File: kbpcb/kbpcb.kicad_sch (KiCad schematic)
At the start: 18 parts

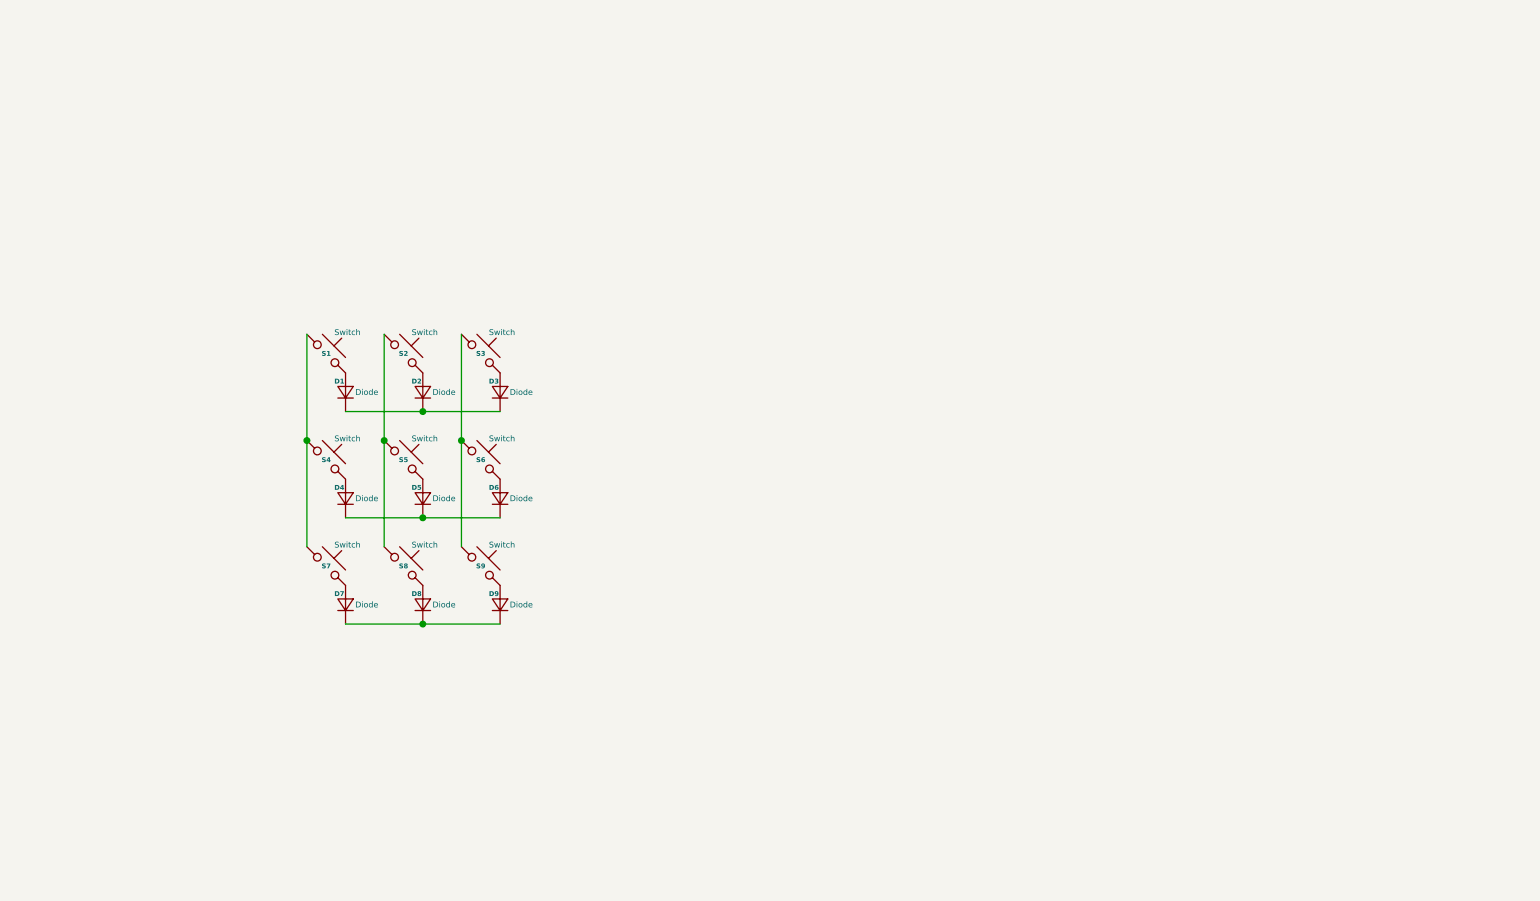
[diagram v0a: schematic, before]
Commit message: placed rp2040 zero and all switches
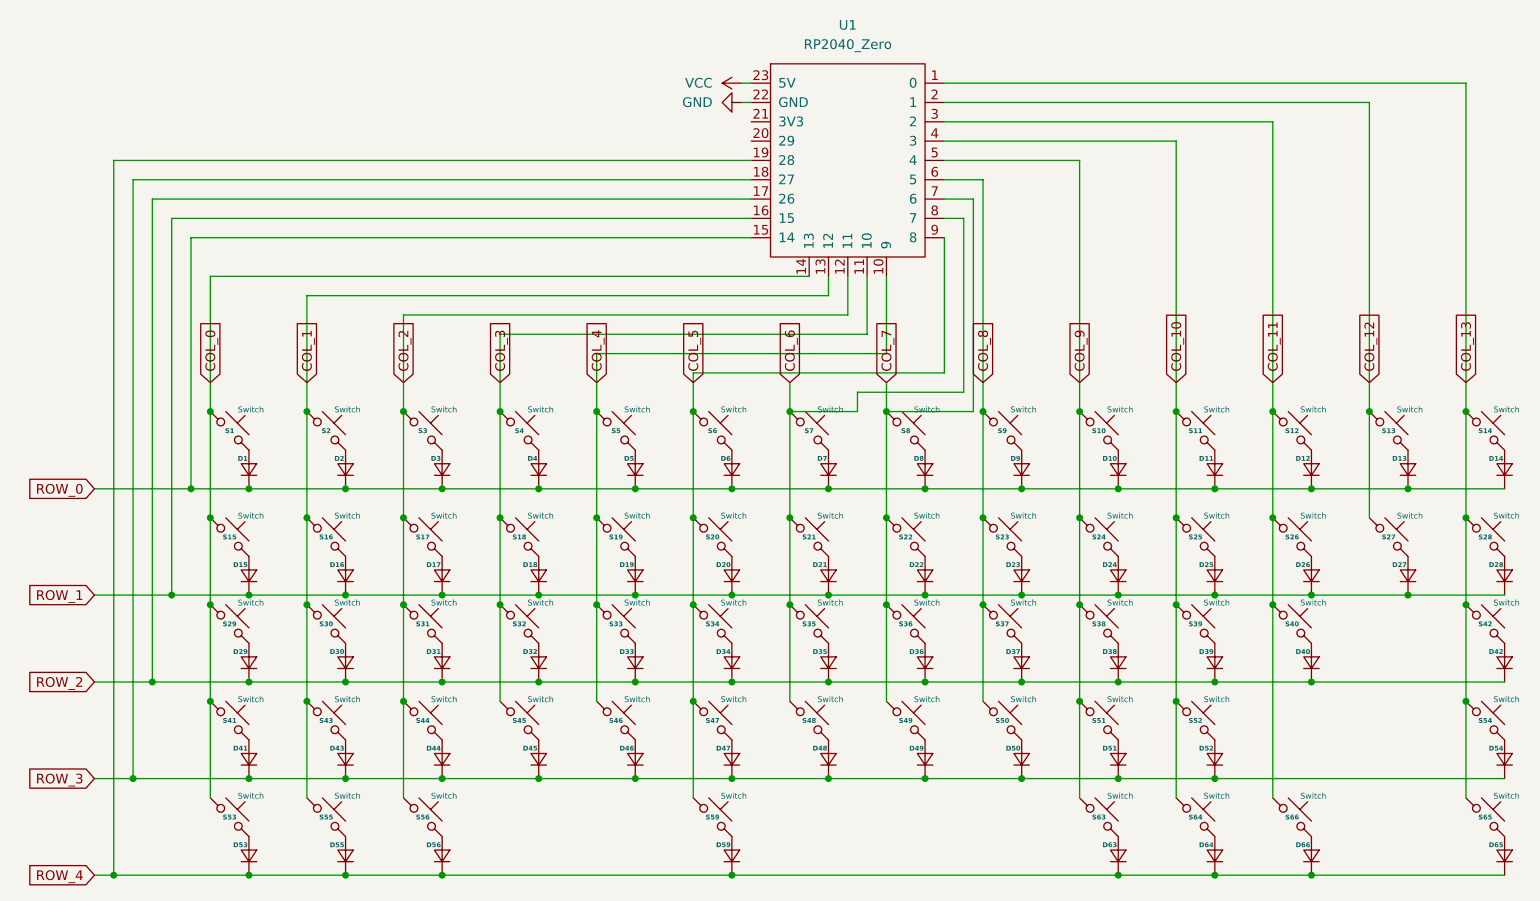
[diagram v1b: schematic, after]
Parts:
- added D10, D11, D12, D13, D14, D15, D16, D17, D18, D19, D20, D21, D22, D23, D24, D25, D26, D27, D28, D29, D30, D31, D32, D33, D34, D35, D36, D37, D38, D39, D40, D41, D42, D43, D44, D45, D46, D47, D48, D49, D50, D51, D52, D53, D54, D55, D56, D59, D63, D64, D65, D66: Diode, Diode_THT:D_DO-35_SOD27_P7.62mm_Horizontal, symbol ScottoKeebs:Placeholder_Diode
- added S10, S11, S12, S13, S14, S15, S16, S17, S18, S19, S20, S21, S22, S23, S24, S25, S26, S27, S28, S29, S30, S31, S32, S33, S34, S35, S36, S37, S38, S39, S40, S41, S42, S43, S44, S45, S46, S47, S48, S49, S50, S51, S52, S53, S54, S55, S56, S59, S63, S64, S65, S66: Switch, CherryMX:CherryMX_1.00u, symbol ScottoKeebs:Placeholder_Keyswitch
- added U1: RP2040_Zero, ScottoKeebs_MCU:RP2040_Zero, symbol ScottoKeebs:MCU_RP2040_Zero
- D1, D2, D3, D4, D5, D6, D7, D8, D9: footprint (none) -> Diode_THT:D_DO-35_SOD27_P7.62mm_Horizontal
- S1, S2, S3, S4, S5, S6, S7, S8, S9: footprint (none) -> CherryMX:CherryMX_1.00u
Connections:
- net ROW_0: now reaches D4.1 (K), D5.1 (K), D6.1 (K)
- net ROW_0: now also D1.1 (K), D2.1 (K), D3.1 (K), D7.1 (K), D8.1 (K), D9.1 (K), D10.1 (K), D11.1 (K), D12.1 (K), D13.1 (K), D14.1 (K), U1.15 (14)
- new net: D51.2 (A), S51.2
- new net: D63.2 (A), S63.2
- new net: D53.2 (A), S53.2
- new net: D21.2 (A), S21.2
- new net: D16.2 (A), S16.2
- new net: D33.2 (A), S33.2
- new net: D55.2 (A), S55.2
- new net: D41.2 (A), S41.2
- new net: D66.2 (A), S66.2
- new net: D34.2 (A), S34.2
- new net: D10.2 (A), S10.2
- new net: D13.2 (A), S13.2
- new net: D36.2 (A), S36.2
- new net: D12.2 (A), S12.2
- new net: D19.2 (A), S19.2
- new net: D42.2 (A), S42.2
- new net: D28.2 (A), S28.2
- new net: D43.2 (A), S43.2
- new net: D49.2 (A), S49.2
- new net: D65.2 (A), S65.2
- new net: D59.2 (A), S59.2
- new net: D26.2 (A), S26.2
- new net: D23.2 (A), S23.2
- new net: D35.2 (A), S35.2
- new net: D24.2 (A), S24.2
- new net: D29.2 (A), S29.2
- new net: D45.2 (A), S45.2
- new net: D27.2 (A), S27.2
- new net: D39.2 (A), S39.2
- new net: D18.2 (A), S18.2
- new net: D37.2 (A), S37.2
- new net: D30.2 (A), S30.2
- new net: D31.2 (A), S31.2
- new net: D20.2 (A), S20.2
- new net: D64.2 (A), S64.2
- new net: D11.2 (A), S11.2
- new net: D40.2 (A), S40.2
- new net: D44.2 (A), S44.2
- new net: D32.2 (A), S32.2
- new net: D54.2 (A), S54.2
- new net: D15.2 (A), S15.2
- new net: D46.2 (A), S46.2
- new net: D17.2 (A), S17.2
- new net: D56.2 (A), S56.2
- new net: D47.2 (A), S47.2
- new net: D52.2 (A), S52.2
- new net: D50.2 (A), S50.2
- new net: D14.2 (A), S14.2
- new net: D25.2 (A), S25.2
- new net: D38.2 (A), S38.2
- new net: D48.2 (A), S48.2
- new net: D22.2 (A), S22.2
- new net COL_0: S1.1, S15.1, S29.1, S41.1, S53.1, U1.14 (13)
- new net COL_1: S16.1, S2.1, S30.1, S43.1, S55.1, U1.13 (12)
- new net COL_10: S11.1, S25.1, S39.1, S52.1, S64.1, U1.4 (3)
- new net COL_11: S12.1, S26.1, S40.1, S66.1, U1.3 (2)
- new net COL_12: S13.1, S27.1, U1.2 (1)
- new net COL_13: S14.1, S28.1, S42.1, S54.1, S65.1, U1.1 (0)
- new net COL_2: S17.1, S3.1, S31.1, S44.1, S56.1, U1.12 (11)
- new net COL_3: S18.1, S32.1, S4.1, S45.1, U1.11 (10)
- new net COL_4: S19.1, S33.1, S46.1, S5.1, U1.10 (9)
- new net COL_5: S20.1, S34.1, S47.1, S59.1, S6.1, U1.9 (8)
- new net COL_6: S21.1, S35.1, S48.1, S7.1, U1.8 (7)
- new net COL_7: S22.1, S36.1, S49.1, S8.1, U1.7 (6)
- new net COL_8: S23.1, S37.1, S50.1, S9.1, U1.6 (5)
- new net COL_9: S10.1, S24.1, S38.1, S51.1, S63.1, U1.5 (4)
- new net GND: U1.22 (GND)
- new net ROW_1: D15.1 (K), D16.1 (K), D17.1 (K), D18.1 (K), D19.1 (K), D20.1 (K), D21.1 (K), D22.1 (K), D23.1 (K), D24.1 (K), D25.1 (K), D26.1 (K), D27.1 (K), D28.1 (K), U1.16 (15)
- new net ROW_2: D29.1 (K), D30.1 (K), D31.1 (K), D32.1 (K), D33.1 (K), D34.1 (K), D35.1 (K), D36.1 (K), D37.1 (K), D38.1 (K), D39.1 (K), D40.1 (K), D42.1 (K), U1.17 (26)
- new net ROW_3: D41.1 (K), D43.1 (K), D44.1 (K), D45.1 (K), D46.1 (K), D47.1 (K), D48.1 (K), D49.1 (K), D50.1 (K), D51.1 (K), D52.1 (K), D54.1 (K), U1.18 (27)
- new net ROW_4: D53.1 (K), D55.1 (K), D56.1 (K), D59.1 (K), D63.1 (K), D64.1 (K), D65.1 (K), D66.1 (K), U1.19 (28)
- new net VCC: U1.23 (5V)
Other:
- moved on the sheet: D1, S1

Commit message: layout changes
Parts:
- removed D54: Diode, Diode_THT:D_DO-35_SOD27_P7.62mm_Horizontal, symbol ScottoKeebs:Placeholder_Diode
- added D1, D100, D101, D102, D103, D104, D105, D106, D107, D108, D109, D110, D111, D112, D113, D114, D115, D116, D117, D118, D119, D120, D121, D122, D123, D124, D125, D126, D127, D128, D129, D130, D131, D132, D133, D134, D135, D136, D137, D138, D139, D140, D141, D142, D143, D144, D145, D146, D147, D148, D149, D150, D151, D152, D153, D154, D155, D156, D157, D158, D159, D160, D161, D162, D163, D164, D165, D166, D167, D168, D169, D170, D171, D172, D173, D174, D175, D176, D177, D178, D179, D180, D181, D182, D183, D184, D185, D186, D187, D188, D189, D2, D3, D4, D41, D5, D55, D56, D57, D6, D60, D61, D63, D64, D69, D7, D70, D71, D72, D73, D74, D75, D76, D77, D78, D79, D8, D80, D81, D82, D83, D84, D85, D86, D87, D88, D89, D90, D91, D92, D93, D94, D95, D96, D97, D98, D99: Diode, Diode_THT:D_DO-35_SOD27_P7.62mm_Horizontal, symbol ScottoKeebs:Placeholder_Diode
- added DS1: OLED_128X64_1.3_I2C, OLED_128X64_1.3_I2C:LCD_OLED_128X64_1.3_I2C, symbol OLED_128X64_1.3_I2C:OLED_128X64_1.3_I2C
- added S1, S100, S101, S102, S103, S104, S105, S106, S107, S108, S109, S110, S111, S112, S113, S114, S115, S116, S117, S118, S119, S120, S121, S122, S123, S124, S125, S126, S127, S128, S129, S130, S131, S132, S133, S134, S135, S136, S137, S138, S139, S140, S141, S142, S143, S144, S145, S146, S147, S148, S149, S150, S151, S152, S153, S154, S155, S156, S157, S158, S159, S160, S161, S162, S163, S164, S165, S166, S167, S168, S169, S170, S171, S172, S173, S174, S175, S176, S177, S178, S179, S180, S181, S182, S183, S184, S185, S186, S187, S188, S189, S2, S3, S4, S41, S5, S55, S56, S6, S60, S61, S63, S64, S69, S7, S70, S71, S72, S73, S74, S75, S76, S77, S78, S79, S8, S80, S81, S82, S83, S84, S85, S86, S87, S88, S89, S90, S91, S92, S93, S94, S95, S96, S97, S98, S99: Switch, CherryMX:CherryMX_1.00u, symbol ScottoKeebs:Placeholder_Keyswitch
- added U2: Teensy4.1, symbol teensy:Teensy4.1
- added U3, U4: TRRS, ScottoKeebs_Components:TRRS_PJ-320A, symbol ScottoKeebs:Placeholder_TRRS
- renumbered D41 to D43, D43 to D44, D44 to D45, D45 to D46, D46 to D47, D47 to D48, D48 to D49, D49 to D50, D50 to D51, D51 to D52, D52 to D53, D53 to D54, D55 to D58, D56 to D59, D59 to D62, D63 to D66, D64 to D67, D66 to D68, S41 to S43, S43 to S44, S44 to S45, S45 to S46, S46 to S47, S47 to S48, S48 to S49, S49 to S50, S50 to S51, S51 to S52, S52 to S53, S53 to S57, S55 to S58, S56 to S59, S59 to S62, S63 to S66, S64 to S67, S66 to S68
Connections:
- net COL_0: now also U1.3 (2), S1.1, S102.1, S110.1, S41.1, S69.1, S78.1, S86.1, S94.1, U2.2 (0_RX1_CRX2_CS1); no longer U1.14 (13)
- net COL_1: now also S54.1, U1.4 (3), S103.1, S111.1, S2.1, S71.1, S79.1, S87.1, S95.1, U2.3 (1_TX1_CTX2_MISO1); no longer U1.13 (12)
- net COL_10: now also U1.14 (13), U2.12 (10_CS_MQSR); no longer U1.4 (3)
- net COL_11: now also U1.15 (14), U2.13 (11_MOSI_CTX1); no longer U1.3 (2)
- net COL_12: now also U1.16 (15), U2.14 (12_MISO_MQSL); no longer U1.2 (1)
- net COL_13: now also U1.17 (26), S56.1, S70.1, U2.36 (14_A0_TX3_SPDIF_OUT); no longer S54.1, S65.1, U1.1 (0)
- net COL_2: now also U1.5 (4), U1.6 (5), S104.1, S112.1, S3.1, S55.1, S72.1, S80.1, S88.1, S96.1, U2.4 (2_OUT2); no longer U1.12 (11)
- net COL_3: now also U1.7 (6), S105.1, S113.1, S4.1, S60.1, S73.1, S81.1, S89.1, S97.1, U2.5 (3_LRCLK2); no longer U1.11 (10)
- net COL_4: now also U1.8 (7), S106.1, S114.1, S5.1, S61.1, S74.1, S82.1, S90.1, S98.1, U2.6 (4_BCLK2); no longer U1.10 (9)
- net COL_5: now also S107.1, S6.1, S63.1, S75.1, S83.1, S91.1, S99.1, U2.7 (5_IN2)
- net COL_6: now also U1.10 (9), S100.1, S108.1, S64.1, S7.1, S76.1, S84.1, S92.1, U2.8 (6_OUT1D); no longer U1.8 (7)
- net COL_7: now also S65.1, U1.11 (10), S101.1, S109.1, S77.1, S8.1, S85.1, S93.1, U2.9 (7_RX2_OUT1A); no longer U1.7 (6)
- net COL_8: now also U1.12 (11), U2.10 (8_TX2_IN1); no longer U1.6 (5)
- net COL_9: now also U1.13 (12), U2.11 (9_OUT1C); no longer U1.5 (4)
- net GND: now also DS1.2 (GND), U2.47 (GND), U4.1 (SLEEVE)
- net ROW_0: now also D1.1 (K), D2.1 (K), D3.1 (K), D4.1 (K), D5.1 (K), D6.1 (K), D7.1 (K), D8.1 (K), U2.37 (15_A1_RX3_SPDIF_IN); no longer U1.15 (14)
- net ROW_1: now also D65.1 (K), D41.1 (K), D55.1 (K), D60.1 (K), D61.1 (K), D63.1 (K), D64.1 (K), D69.1 (K), U2.38 (16_A2_RX4_SCL1); no longer U1.16 (15)
- net ROW_2: now also D71.1 (K), D72.1 (K), D73.1 (K), D74.1 (K), D75.1 (K), D76.1 (K), D77.1 (K), D78.1 (K), U2.39 (17_A3_TX4_SDA1); no longer U1.17 (26)
- net ROW_3: now also D56.1 (K), D79.1 (K), D80.1 (K), D81.1 (K), D82.1 (K), D83.1 (K), D84.1 (K), D85.1 (K), D86.1 (K), U2.40 (18_A4_SDA); no longer U1.18 (27)
- net ROW_4: now also D70.1 (K), D87.1 (K), D88.1 (K), D89.1 (K), D90.1 (K), D91.1 (K), D92.1 (K), D93.1 (K), D94.1 (K), U2.41 (19_A5_SCL); no longer D65.1 (K), U1.19 (28)
- net VCC: now also U2.48 (VIN), U4.2 (TIP); no longer U1.23 (5V)
- net at S65.2: now also D69.2 (A); no longer D65.2 (A)
- net at S54.2: now also D55.2 (A)
- net +3V3: now reaches U1.21 (3V3)
- new net: D144.2 (A), S143.2
- new net: D173.2 (A), S172.2
- new net: D100.2 (A), S99.2
- new net: D72.2 (A), S71.2
- new net: D183.2 (A), S183.2
- new net: D168.2 (A), S167.2
- new net: D103.2 (A), S102.2
- new net: D94.2 (A), S93.2
- new net: D83.2 (A), S82.2
- new net: D139.2 (A), S138.2
- new net: D70.2 (A), S70.2
- new net: D99.2 (A), S98.2
- new net: D175.2 (A), S174.2
- new net: D121.2 (A), S120.2
- new net: D177.2 (A), S176.2
- new net: D153.2 (A), S152.2
- new net: D90.2 (A), S89.2
- new net: D117.2 (A), S116.2
- new net: D64.2 (A), S63.2
- new net: D2.2 (A), S2.2
- new net: D160.2 (A), S159.2
- new net: D114.2 (A), S113.2
- new net: D170.2 (A), S169.2
- new net: D187.2 (A), S187.2
- new net: D76.2 (A), S75.2
- new net: D60.2 (A), S55.2
- new net: D124.2 (A), S123.2
- new net: D128.2 (A), S127.2
- new net: D1.2 (A), S1.2
- new net: D88.2 (A), S87.2
- new net: D123.2 (A), S122.2
- new net: D135.2 (A), S134.2
- new net: D41.2 (A), S41.2
- new net: D112.2 (A), S111.2
- new net: D148.2 (A), S147.2
- new net: D151.2 (A), S150.2
- new net: D181.2 (A), S180.2
- new net: D113.2 (A), S112.2
- new net: D115.2 (A), S114.2
- new net: D57.2 (A), S181.2
- new net: D184.2 (A), S184.2
- new net: D159.2 (A), S158.2
- new net: D86.2 (A), S85.2
- new net: D155.2 (A), S154.2
- new net: D85.2 (A), S84.2
- new net: D152.2 (A), S151.2
- new net: D166.2 (A), S165.2
- new net: D163.2 (A), S162.2
- new net: D141.2 (A), S140.2
- new net: D108.2 (A), S107.2
- new net: D106.2 (A), S105.2
- new net: D116.2 (A), S115.2
- new net: D127.2 (A), S126.2
- new net: D133.2 (A), S132.2
- new net: D161.2 (A), S160.2
- new net: D129.2 (A), S128.2
- new net: D92.2 (A), S91.2
- new net: D7.2 (A), S7.2
- new net: D5.2 (A), S5.2
- new net: D178.2 (A), S177.2
- new net: D101.2 (A), S100.2
- new net: D179.2 (A), S178.2
- new net: D130.2 (A), S129.2
- new net: S124.1, S130.1, S136.1, S142.1, S148.1
- new net: D125.2 (A), S124.2
- new net: D138.2 (A), S137.2
- new net: D176.2 (A), S175.2
- new net: D180.2 (A), S179.2
- new net: D165.2 (A), S164.2
- new net: D105.2 (A), S104.2
- new net: D146.2 (A), S145.2
- new net: D174.2 (A), S173.2
- new net: D188.2 (A), S188.2
- new net: D78.2 (A), S77.2
- new net: D118.2 (A), S117.2
- new net: D79.2 (A), S78.2
- new net: D56.2 (A), S56.2
- new net: D63.2 (A), S61.2
- new net: D150.2 (A), S149.2
- new net: D75.2 (A), S74.2
- new net: D134.2 (A), S133.2
- new net: D102.2 (A), S101.2
- new net: D149.2 (A), S148.2
- new net: D96.2 (A), S95.2
- new net: D122.2 (A), S121.2
- new net: D77.2 (A), S76.2
- new net: D137.2 (A), S136.2
- new net: D91.2 (A), S90.2
- new net: D164.2 (A), S163.2
- new net: D110.2 (A), S109.2
- new net: D104.2 (A), S103.2
- new net: D158.2 (A), S157.2
- new net: D172.2 (A), S171.2
- new net: D87.2 (A), S86.2
- new net: D189.2 (A), S189.2
- new net: D81.2 (A), S80.2
- new net: D71.2 (A), S69.2
- new net: D136.2 (A), S135.2
- new net: D157.2 (A), S156.2
- new net: D74.2 (A), S73.2
- new net: D6.2 (A), S6.2
- new net: D84.2 (A), S83.2
- new net: D132.2 (A), S131.2
- new net: D4.2 (A), S4.2
- new net: D111.2 (A), S110.2
- new net: D97.2 (A), S96.2
- new net: D182.2 (A), S182.2
- new net: D80.2 (A), S79.2
- new net: D167.2 (A), S166.2
- new net: D131.2 (A), S130.2
- new net: D185.2 (A), S185.2
- new net: D186.2 (A), S186.2
- new net: D8.2 (A), S8.2
- new net: D162.2 (A), S161.2
- new net: D142.2 (A), S141.2
- new net: D73.2 (A), S72.2
- new net: D65.2 (A), S64.2
- new net: D143.2 (A), S142.2
- new net: D126.2 (A), S125.2
- new net: D120.2 (A), S119.2
- new net: D169.2 (A), S168.2
- new net: D171.2 (A), S170.2
- new net: D61.2 (A), S60.2
- new net: D93.2 (A), S92.2
- new net: D109.2 (A), S108.2
- new net: D98.2 (A), S97.2
- new net: D95.2 (A), S94.2
- new net: D147.2 (A), S146.2
- new net: D107.2 (A), S106.2
- new net: D89.2 (A), S88.2
- new net: D3.2 (A), S3.2
- new net: D154.2 (A), S153.2
- new net: D119.2 (A), S118.2
- new net: D156.2 (A), S155.2
- new net: D140.2 (A), S139.2
- new net: D145.2 (A), S144.2
- new net: D82.2 (A), S81.2
- new net LEFT_COL_0: S176.1, S181.1, S182.1, S183.1
- new net LEFT_COL_1: S174.1, S175.1, S177.1, S178.1, S180.1, S184.1, S185.1, S186.1
- new net LEFT_COL_2: S169.1, S170.1, S171.1, S172.1, S173.1, S187.1, S188.1, S189.1
- new net LEFT_COL_3: S165.1, S166.1, S167.1, S168.1, S179.1
- new net LEFT_COL_4: S160.1, S161.1, S162.1, S163.1, S164.1
- new net LEFT_COL_5: S155.1, S156.1, S157.1, S158.1, S159.1
- new net LEFT_COL_6: S150.1, S151.1, S152.1, S153.1, S154.1
- new net LEFT_COL_7: S131.1, S137.1, S143.1, S147.1, S149.1
- new net LEFT_ROW_0: D132.1 (K), D151.1 (K), D156.1 (K), D161.1 (K), D166.1 (K), D170.1 (K), D175.1 (K), D184.1 (K), D187.1 (K), D57.1 (K)
- new net LEFT_ROW_1: D138.1 (K), D152.1 (K), D157.1 (K), D162.1 (K), D167.1 (K), D171.1 (K), D176.1 (K), D177.1 (K), D182.1 (K), D185.1 (K), D188.1 (K)
- new net LEFT_ROW_2: D144.1 (K), D153.1 (K), D158.1 (K), D163.1 (K), D168.1 (K), D172.1 (K), D178.1 (K), D183.1 (K), D186.1 (K), D189.1 (K)
- new net LEFT_ROW_3: D148.1 (K), D154.1 (K), D159.1 (K), D164.1 (K), D169.1 (K), D173.1 (K), D179.1 (K)
- new net LEFT_ROW_4: D150.1 (K), D155.1 (K), D160.1 (K), D165.1 (K), D174.1 (K), D180.1 (K), D181.1 (K)
- new net MID_COL_0: S115.1, S116.1, S117.1, S118.1, S119.1
- new net MID_COL_1: S120.1, S126.1, S132.1, S138.1, S144.1
- new net MID_COL_2: S121.1, S127.1, S133.1, S139.1, S145.1
- new net MID_COL_3: S122.1, S128.1, S134.1, S140.1, S146.1
- new net MID_COL_4: S123.1, S129.1, S135.1, S141.1
- new net MID_COL_6: S125.1
- new net MID_ROW_0: D116.1 (K), D121.1 (K), D122.1 (K), D123.1 (K), D124.1 (K), D125.1 (K), D126.1 (K)
- new net MID_ROW_1: D117.1 (K), D127.1 (K), D128.1 (K), D129.1 (K), D130.1 (K), D131.1 (K)
- new net MID_ROW_2: D118.1 (K), D133.1 (K), D134.1 (K), D135.1 (K), D136.1 (K), D137.1 (K)
- new net MID_ROW_3: D119.1 (K), D139.1 (K), D140.1 (K), D141.1 (K), D142.1 (K), D143.1 (K)
- new net MID_ROW_4: D120.1 (K), D145.1 (K), D146.1 (K), D147.1 (K), D149.1 (K)
- new net OLED_3V3: U2.15 (3V3)
- new net OLED_SCL: DS1.3 (SCK), U2.16 (24_A10_TX6_SCL2)
- new net OLED_SDA: DS1.4 (SDA), U2.17 (25_A11_RX6_SDA2)
- new net RIGHT_SCL: U1.2 (1), U4.4 (RING2)
- new net RIGHT_SDA: U1.1 (0), U4.3 (RING1)
- new net ROW_5: D100.1 (K), D101.1 (K), D102.1 (K), D95.1 (K), D96.1 (K), D97.1 (K), D98.1 (K), D99.1 (K)
- new net ROW_6: D103.1 (K), D104.1 (K), D105.1 (K), D106.1 (K), D107.1 (K), D108.1 (K), D109.1 (K), D110.1 (K)
- new net ROW_7: D111.1 (K), D112.1 (K), D113.1 (K), D114.1 (K), D115.1 (K)
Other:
- note added: "8-0, -, =, back, tab, q"
- note added: "enter, shft, z-n"
- note added: "esc, 1-7"
- note added: "f-l, ;, '"
- note added: "m, <, >, ?, shft, ctrl, win, alt"
- note added: "p, [, ], \, caps, a-d"
- note added: "space, rALT, fn, fn2, rCTRL"
- note added: "w-o"
- moved on the sheet: D1, D10, D11, D12, D13, D15, D16, D17, D18, D19, D2, D20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
